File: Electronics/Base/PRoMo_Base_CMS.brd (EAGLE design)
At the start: 48 x 98 mm, 40 parts, among them IC1 DSPIC33FJ128MC804-PT, IC2 LM1117IMPX-3.3, IC3 FT232RL, J1 CON Jack, P1 Bornier, X1 PN61729-S

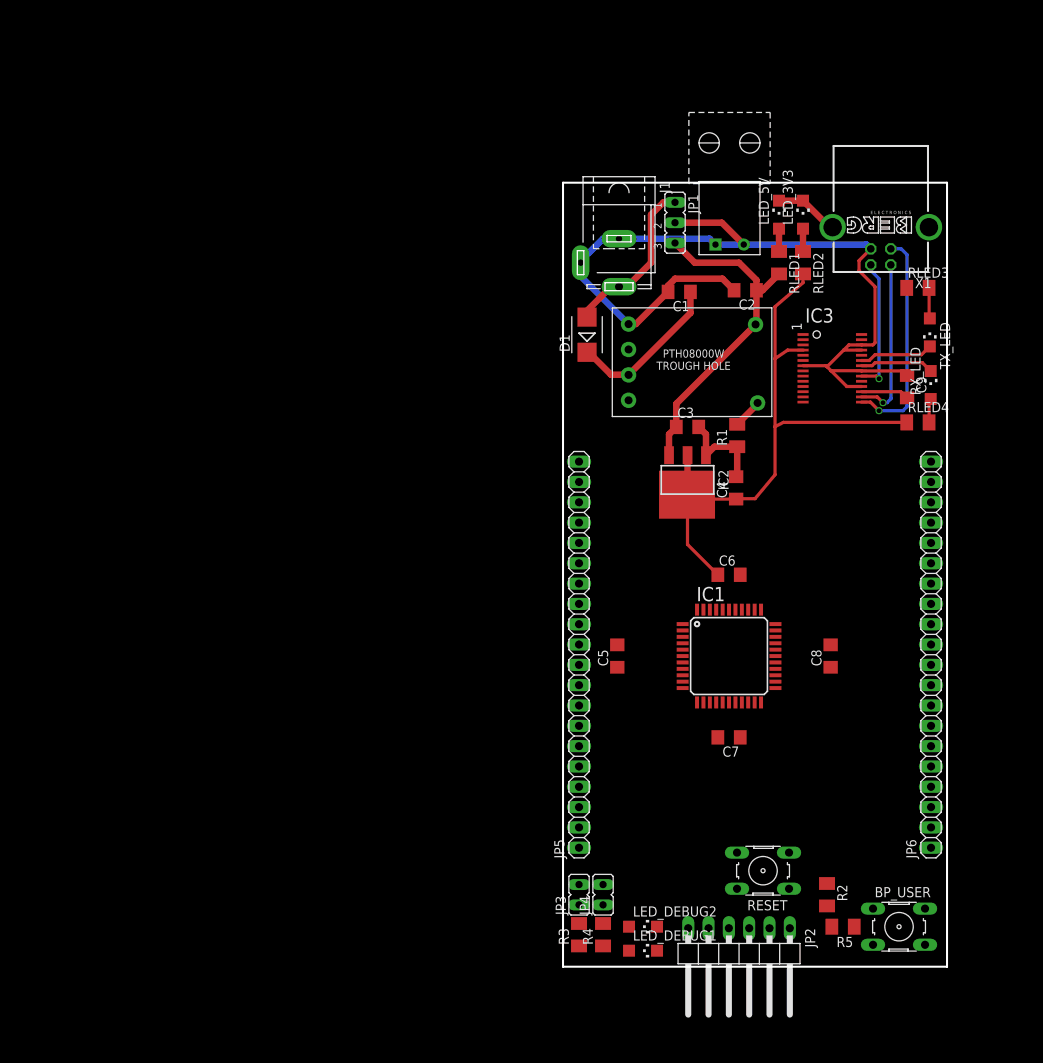
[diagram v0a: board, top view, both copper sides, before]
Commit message: Utilisation Lib SeeedStudio
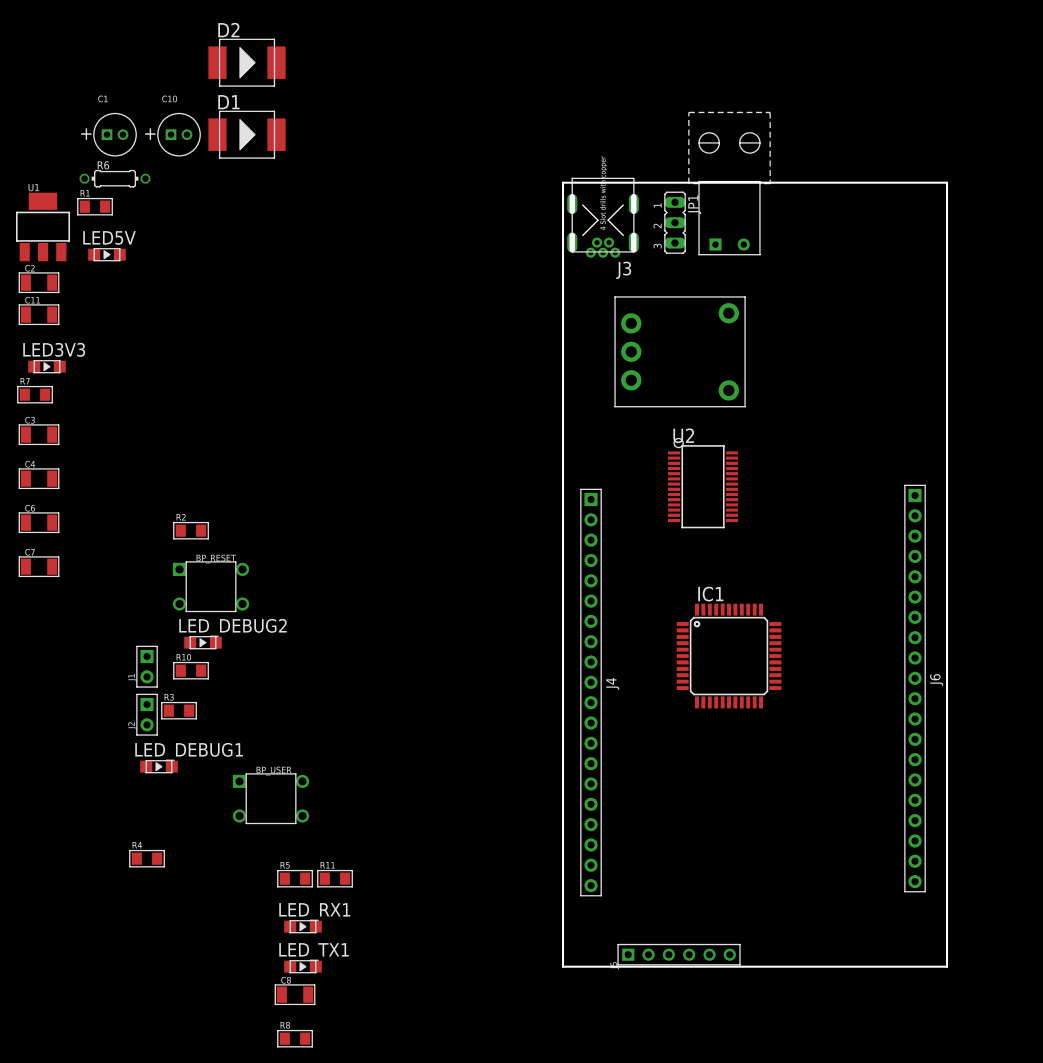
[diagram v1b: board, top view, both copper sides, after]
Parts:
- removed C5: 10µF, resistor:C1206
- removed C9: 100nF, resistor:C1206
- removed IC2: LM1117IMPX-3.3, lm1117:SOT223
- removed IC3: FT232RL, ftdichip-3:SSOP28DB
- removed JP2: PICKit, pinhead:1X06/90
- removed JP3, JP4: (no value), jumper:JP1
- removed JP5, JP6: (no value), pinhead:1X20
- removed LED_3V3, LED_5V, RX_LED, TX_LED: (no value), led:CHIPLED_1206
- removed RESET: (no value), switch-omron:B3F-10XX
- removed RLED1, RLED2, RLED3, RLED4: 56, resistor:M1206
- removed X1: PN61729-S, con-berg:PN61729-S
- added BP_RESET: (no value), Discrete:4P-6.2X6.2
- added C10: 100µF, Discrete:ELECTRO-5.3MM
- added C11: 10µF, Discrete:C1206
- added D2: (no value), Discrete:DO-214AB
- added J2: (no value), Connector :2P-2.54-65/35MIL
- added J3: (no value), Connector :MINI-5P
- added J4, J6: (no value), Connector :20P-2.54
- added J5: (no value), Connector :6P-2.54-60/35MIL
- added LED3V3, LED5V, LED_RX1, LED_TX1: (no value), Discrete:LED-1206
- added R10, R11, R7: 56, Discrete:R1206
- added R6: 353, Discrete:R0204/7
- added R8: 10k, Discrete:R1206
- added U1: CJ1117-3.3-1310190P1, OPL:SOT223
- added U2: FT232R-SSOP28, IC:SSOP28
- BP_USER: device switch-omron:B3F-10XX -> Discrete:4P-6.2X6.2
- C1: device resistor:C1206 -> Discrete:ELECTRO-5.3MM
- C2: value 100µF -> 100nF; device resistor:C1206 -> Discrete:C1206
- C3, C6, C8: device resistor:C1206 -> Discrete:C1206
- C4: value 10µF -> 100nF; device resistor:C1206 -> Discrete:C1206
- C7: value 100nF -> 10µF; device resistor:C1206 -> Discrete:C1206
- D1: value B130LB -> (none); device diode:SMB -> Discrete:DO-214AB
- J1: value CON Jack -> (none); device con-jack:SPC4078 -> Connector :2P-2.54-65/35MIL
- LED_DEBUG1, LED_DEBUG2: device led:CHIPLED_1206 -> Discrete:LED-1206
- R1, R3: value 353 -> 56; device resistor:M1206 -> Discrete:R1206
- R2: device resistor:M1206 -> Discrete:R1206
- R4: value 353 -> 10k; device resistor:M1206 -> Discrete:R1206
- R5: value 10k -> 56; device resistor:M1206 -> Discrete:R1206
- REG1: value (none) -> PTH08080W; device Perso:TRHOUGH_HOLE_(EUS) -> Perso:PTH08080W
- moved R2 91.6 mm to (-46.5, 54.5), turned to 0 degrees
- moved C7 88.8 mm to (-65.5, 50.0), turned to 0 degrees
- moved C2 88.3 mm to (-65.5, 85.5), turned to 0 degrees
- moved C4 87.1 mm to (-65.5, 61.0), turned to 0 degrees
- moved C6 86.5 mm to (-65.5, 55.5)
- moved R1 85.2 mm to (-58.5, 95.0), turned to 0 degrees
- moved C3 81.1 mm to (-65.5, 66.5)
- moved BP_USER 80.1 mm to (-36.5, 21.0)
- moved C8 79.2 mm to (-33.5, -3.50), turned to 0 degrees
- moved J1 77.7 mm to (-52.0, 37.5), turned to 0 degrees
- moved C1 73.2 mm to (-56.0, 104.0), turned to 0 degrees
- moved R5 68.8 mm to (-33.5, 11.0), turned to 0 degrees
- moved LED_DEBUG2 65.5 mm to (-45.0, 40.5), turned to 0 degrees
- moved LED_DEBUG1 64.7 mm to (-50.5, 25.0), turned to 0 degrees
- moved R4 57.8 mm to (-52.0, 13.5), turned to 0 degrees
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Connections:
- removed net N$10: RLED3.2, TX_LED.A
- removed net N$11: RLED4.2, RX_LED.A
- removed net N$12: IC3.22, RX_LED.C
- removed net N$13: C9.2, IC3.17
- new net N$17: LED_TX1.+, R5.1
- new net N$18: LED_RX1.+, R11.1
- new net N$19: LED_RX1.-, U2.22
- new net N$6: J2.1, R3.2
- new net N$8: C8.2, U2.17
- net !MCLR!: now also BP_RESET.1, BP_RESET.4, J5.1; no longer JP2.1, RESET.1, RESET.2
- net +3V3: now also C11.1, C3.1, J5.2, R11.2, R4.2, R7.1, U1.2, U1.TER, U2.4; no longer C7.1, C8.1, IC2.2, IC2.TAB, IC3.4, JP2.2, RLED2.2, RLED3.1, RLED4.1
- net +5V: now also C1.+, D2.1, J3.VCC, R1.1, R8.1, REG1.P$5, U1.3, U2.20; no longer C3.1, IC2.3, IC3.20, REG1.6, RLED1.2, X1.1
- net BP_USER: now also BP_USER.4, R4.1; no longer BP_USER.2, R5.1
- net D+: now also J3.DP, U2.15; no longer IC3.15, X1.3
- net D-: now also J3.DM, U2.16; no longer IC3.16, X1.2
- net LED_DEBUG1: now also J2.2; no longer JP3.2
- net LED_DEBUG2: now also J1.2; no longer JP4.2
- net N$1: now also C10.+, D1.2, D2.2, REG1.P$1; no longer C1.1, D1.C, REG1.3
- net N$14: now also LED_DEBUG2.+, R10.1; no longer LED_DEBUG2.A, R4.1
- net N$15: now also LED_TX1.-, U2.23; no longer JP3.1, R3.2
- net N$16: now also J1.1, R10.2; no longer JP4.1, R4.2
- net N$2: now also R6.2, REG1.P$4; no longer R1.2, REG1.5
- net N$3: now also LED5V.+, R1.2; no longer LED_5V.A, RLED1.1
- net N$5: now also LED_DEBUG1.+; no longer LED_DEBUG1.A
- net N$7: now also LED3V3.+, R7.2; no longer LED_3V3.A, RLED2.1
- net N$9: now also R8.2, U2.19; no longer IC3.23, TX_LED.C
- net PE: now also BP_RESET.2, BP_RESET.3, BP_USER.2, C1.-, C10.-, C11.2, C8.1, J3.GND, J3.S1, J3.S2, J3.S3, J3.S4, J5.3, LED3V3.-, LED5V.-, LED_DEBUG1.-, LED_DEBUG2.-, R6.1, REG1.P$3, U1.1, U2.18, U2.21, U2.25, U2.26, U2.7; no longer BP_USER.4, C1.2, C5.2, C8.2, C9.1, IC2.1, IC3.18, IC3.21, IC3.25, IC3.26, IC3.7, J1.1, J1.2, JP2.3, LED_3V3.C, LED_5V.C, LED_DEBUG1.C, LED_DEBUG2.C, R1.1, REG1.1, RESET.3, RESET.4, X1.4, X1.S1, X1.S2
- net PGEC: now also J5.5; no longer JP2.5
- net PGED: now also J5.4; no longer JP2.4
- net RX: now also U2.1; no longer IC3.1
- net TX: now also U2.5; no longer IC3.5
- net V+: now also D1.1; no longer D1.A, J1.3
- net VCAP: now also C7.1; no longer C5.1
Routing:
- net PE: track 126.6 -> 0.00 mm
- net +3V3: track 76.3 -> 0.00 mm
- net +5V: track 59.1 -> 0.00 mm, vias 1 -> 0
- net D+: track 27.7 -> 0.00 mm, vias 1 -> 0
- net D-: track 20.9 -> 0.00 mm, vias 1 -> 0
- net V+: track 20.9 -> 0.00 mm
- net N$1: track 19.9 -> 0.00 mm
- net N$4: track 9.72 -> 0.00 mm
- net N$9: track 9.27 -> 0.00 mm
- net N$12: track 9.23 -> 0.00 mm
- net N$13: track 6.01 -> 0.00 mm
- net N$10: track 3.85 -> 0.00 mm
- net N$2: track 3.73 -> 0.00 mm
- net N$11: track 3.00 -> 0.00 mm
- net N$7: track 2.85 -> 0.00 mm
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
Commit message: Schématique OK, début routage
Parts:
- removed J1, J2: (no value), Connector :2P-2.54-65/35MIL
- removed J4, J6: (no value), Connector :20P-2.54
- removed J5: (no value), Connector :6P-2.54-60/35MIL
- added JP2: (no value), pinhead:1X22
- added JP3: (no value), jumper:JP2Q
- added JP4: (no value), pinhead:1X06/90
- added JP5: (no value), jumper:JP3Q
- added Q1: (no value), Discrete:SOT23
- added R12, R23, R24, R9: (no value), Discrete:R0805
- C11, C2, C3, C4, C6, C7, C8: device Discrete:C1206 -> Discrete:C0805
- D1, D2: device Discrete:DO-214AB -> Discrete:SOD123
- JP1: device jumper:JP2 -> pinhead:1X22
- R1, R10, R11, R2, R3, R4, R5, R7, R8: device Discrete:R1206 -> Discrete:R0805
- moved LED_TX1 117.5 mm to (44.1, 89.1), turned to 180 degrees
- moved LED_RX1 111.8 mm to (44.0, 86.5), turned to 180 degrees
- moved LED3V3 110.0 mm to (44.2, 92.0)
- moved R7 106.6 mm to (38.6, 92.0)
- moved R5 106.4 mm to (38.7, 89.1)
- moved C4 106.1 mm to (37.0, 33.6), turned to 180 degrees
- moved C11 103.5 mm to (38.0, 80.5), turned to 90 degrees
- moved R11 101.5 mm to (40.3, 85.6), turned to 90 degrees
- moved LED5V 101.3 mm to (44.1, 94.7)
- moved C3 100.4 mm to (23.8, 20.6), turned to 270 degrees
- moved U1 98.7 mm to (33.0, 80.5), turned to 180 degrees
- moved LED_DEBUG1 98.2 mm to (45.0, 2.00)
- moved R1 97.1 mm to (38.6, 94.8)
- moved LED_DEBUG2 96.7 mm to (45.0, 5.00)
- moved C2 93.1 mm to (27.5, 89.0), turned to 90 degrees
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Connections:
- removed net AN0: IC1.19
- removed net AN1: IC1.20
- removed net AN4: IC1.23
- removed net AN5/MISO: IC1.24
- removed net AN6/MOSI: IC1.25
- removed net AN7/CSN: IC1.26
- removed net AN8/SCK: IC1.27
- removed net BP_USER: BP_USER.1, BP_USER.4, IC1.30, R4.1
- removed net LED_DEBUG1: IC1.31, J2.2
- removed net LED_DEBUG2: IC1.32, J1.2
- removed net N$1: C10.+, D1.2, D2.2, REG1.P$1
- removed net N$18: LED_RX1.+, R11.1
- removed net N$19: LED_RX1.-, U2.22
- removed net N$25: IC1.33
- removed net N$26: IC1.34
- removed net N$27: IC1.35
- removed net N$28: IC1.36
- removed net N$4: JP1.2, P1.VCC
- removed net PWM1H: IC1.14
- removed net PWM1L: IC1.15
- removed net PWM2H: IC1.10
- removed net PWM2L: IC1.11
- removed net PWM3H/GPIO: IC1.2
- removed net PWM3L/GPIO: IC1.3
- removed net QE1A: IC1.9
- removed net QE1B: IC1.8
- removed net QE2A: IC1.5
- removed net QE2B: IC1.4
- removed net RX: IC1.38, U2.1
- removed net SDA/GPIO: IC1.41
- removed net SDL/GPIO: IC1.42
- removed net SENS1: IC1.13
- removed net SENS2: IC1.12
- removed net SENS3/GPIO: IC1.1
- removed net TX: IC1.37, U2.5
- removed net UART2_: IC1.44
- removed net UART2_AX12: IC1.43
- new net AN0/RA0: IC1.19, JP3.1, R12.2, R9.2
- new net AN1/RA1: IC1.20, JP3.3, R23.2, R24.2
- new net AN4/RP2/RB2: IC1.23, JP2.18
- new net AN5/MISO/RP3/RB3: IC1.24, JP2.19
- new net AN6/MOSI/RP16/RC0: IC1.25, JP2.20
- new net AN7/CSN/RP17/RC1: IC1.26, JP2.21
- new net AN8/SCK/RP18/RC2: IC1.27, JP2.22
- new net BP: BP_USER.1, BP_USER.4, JP5.5, R4.1
- new net BP_USER/RA8: IC1.32, JP1.20, JP5.6
- new net LED_DEBUG1/RA2: IC1.30, JP1.22
- new net LED_DEBUG2/RA3: IC1.31, JP1.21, JP5.4
- new net N$10: JP2.17, JP3.4, R23.1
- new net N$11: JP2.16, JP3.2, R9.1
- new net N$12: R11.1, U2.22
- new net N$13: R5.1, U2.23
- new net PWM1H/RP14/RB14: IC1.14, JP2.14
- new net PWM1L/RP14/RB15: IC1.15, JP2.15
- new net PWM2H/RP12/RB12: IC1.10, JP2.10
- new net PWM2L/RP13/RB13: IC1.11, JP2.11
- new net PWM3H/RP22: IC1.2, JP1.8
- new net PWM3L/RP23: IC1.3, JP1.7
- new net QE1A/RP11/RB11: IC1.9, JP2.9
- new net QE1B/RP10/RB10: IC1.8, JP2.8
- new net QE2A/RP25/RC9: IC1.5, JP2.7
- new net QE2B/RP24/RC8: IC1.4, JP2.6
- new net RA4: IC1.34, JP1.18
- new net RA9: IC1.35, JP1.17
- new net RP21/RC5: IC1.38, JP1.14
- new net RP4/RB4: IC1.33, JP1.19
- new net RX_FTDI: IC1.43, JP1.10, U2.1
- new net SDA/RP5/RB5: IC1.41, JP1.13
- new net SDL/RP6/RB6: IC1.42, JP1.12
- new net SENS1/RA7: IC1.13, JP2.13
- new net SENS2/RA10: IC1.12, JP2.12
- new net SENS3/RP9/RB9: IC1.1, JP1.9
- new net TX_FTDI: IC1.44, JP1.11, U2.5
- new net UART_AX12/RP19/RC3: IC1.36, JP1.16
- new net UART_BIS/RP20/RC4: IC1.37, JP1.15
- new net VIN: C10.+, D1.-, D2.-, JP2.1, JP2.2, Q1.1, REG1.P$1
- new net VUSB: J3.VCC, Q1.3
- net !MCLR!: now also JP4.6; no longer J5.1
- net +3V3: now also JP1.3, JP1.4, JP4.5, LED_RX1.+, LED_TX1.+; no longer J5.2, R11.2, R5.2
- net +5V: now also D2.+, JP1.1, JP1.2, Q1.2, REG1.P$3; no longer D2.1, J3.VCC, JP1.3, REG1.P$5
- net N$15: now also R5.2; no longer U2.23
- net N$16: now also JP5.3; no longer J1.1
- net N$17: now also LED_RX1.-, R11.2; no longer LED_TX1.+, R5.1
- net N$6: now also JP5.1; no longer J2.1
- net PE: now also JP1.5, JP1.6, JP2.3, JP2.4, JP2.5, JP4.4, R12.1, R24.1, REG1.P$2; no longer J5.3, REG1.P$3
- net PGEC: now also JP4.2; no longer J5.5
- net PGED: now also JP4.3; no longer J5.4
- net V+: now also D1.+, P1.VCC; no longer D1.1, JP1.1
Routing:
- net PE: track 0.00 -> 230.0 mm, vias 0 -> 7
- net +3V3: track 0.00 -> 63.8 mm
- net VIN: track 0.00 -> 57.8 mm
- net +5V: track 0.00 -> 57.5 mm
- net D-: track 0.00 -> 37.5 mm, vias 0 -> 1
- net QE2B/RP24/RC8: track 0.00 -> 35.9 mm
- net QE2A/RP25/RC9: track 0.00 -> 33.4 mm
- net D+: track 0.00 -> 30.4 mm, vias 0 -> 1
- net AN8/SCK/RP18/RC2: track 0.00 -> 29.7 mm
- net PGED: track 0.00 -> 29.4 mm, vias 0 -> 2
- net AN7/CSN/RP17/RC1: track 0.00 -> 27.3 mm
- net PGEC: track 0.00 -> 27.2 mm, vias 0 -> 2
- net QE1B/RP10/RB10: track 0.00 -> 25.6 mm
- net PWM3L/RP23: track 0.00 -> 25.5 mm
- net AN6/MOSI/RP16/RC0: track 0.00 -> 25.0 mm
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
